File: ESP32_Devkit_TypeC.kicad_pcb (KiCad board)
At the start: 2 copper layers, 25.3 x 48.2 mm, 39 parts, among them J1 USB_C_Receptacle_USB2.0, J2 Conn_01x19, J3 Conn_01x19, Q1 SS8050, Q2 SS8050, SW1 EN, SW2 BOOT, U1 MP2451, U2 CH340G, U3 ESP32-PICO-D4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

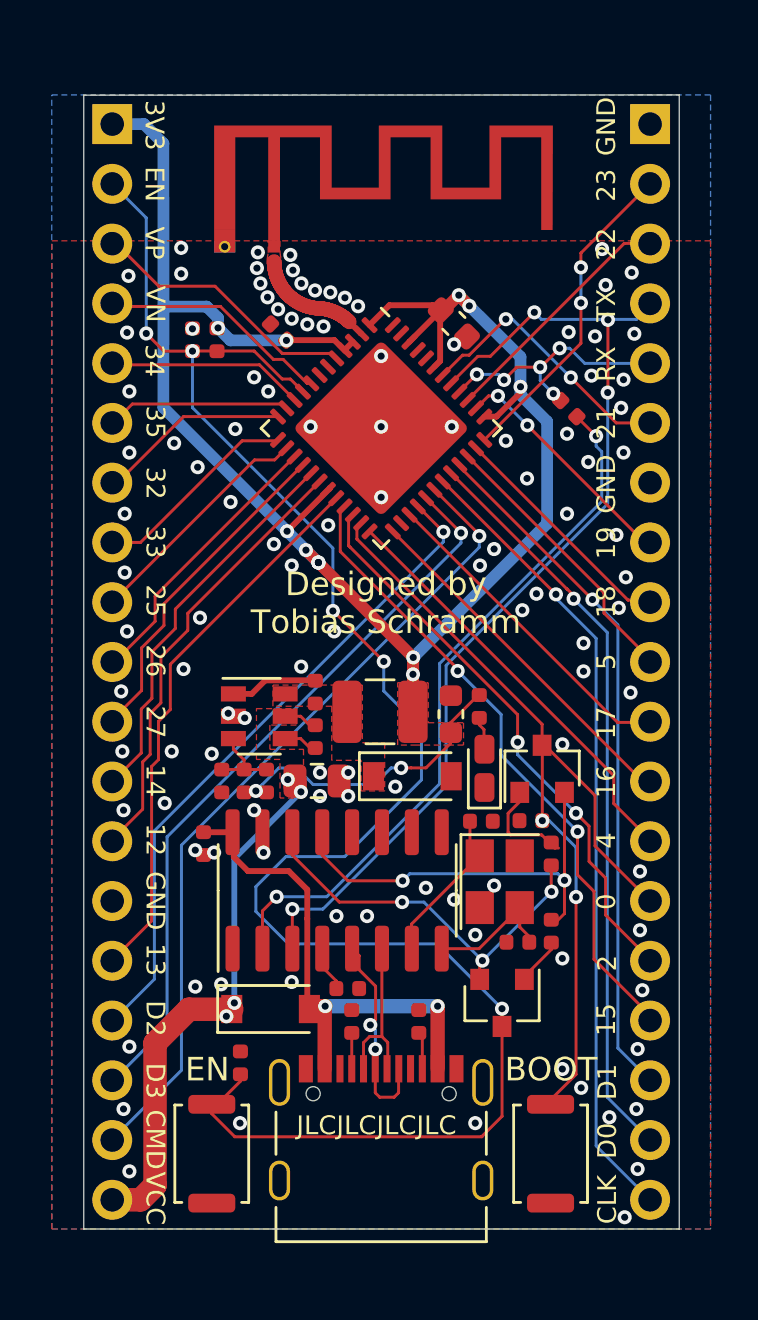
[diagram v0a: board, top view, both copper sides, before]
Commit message: Add silkscreen markings
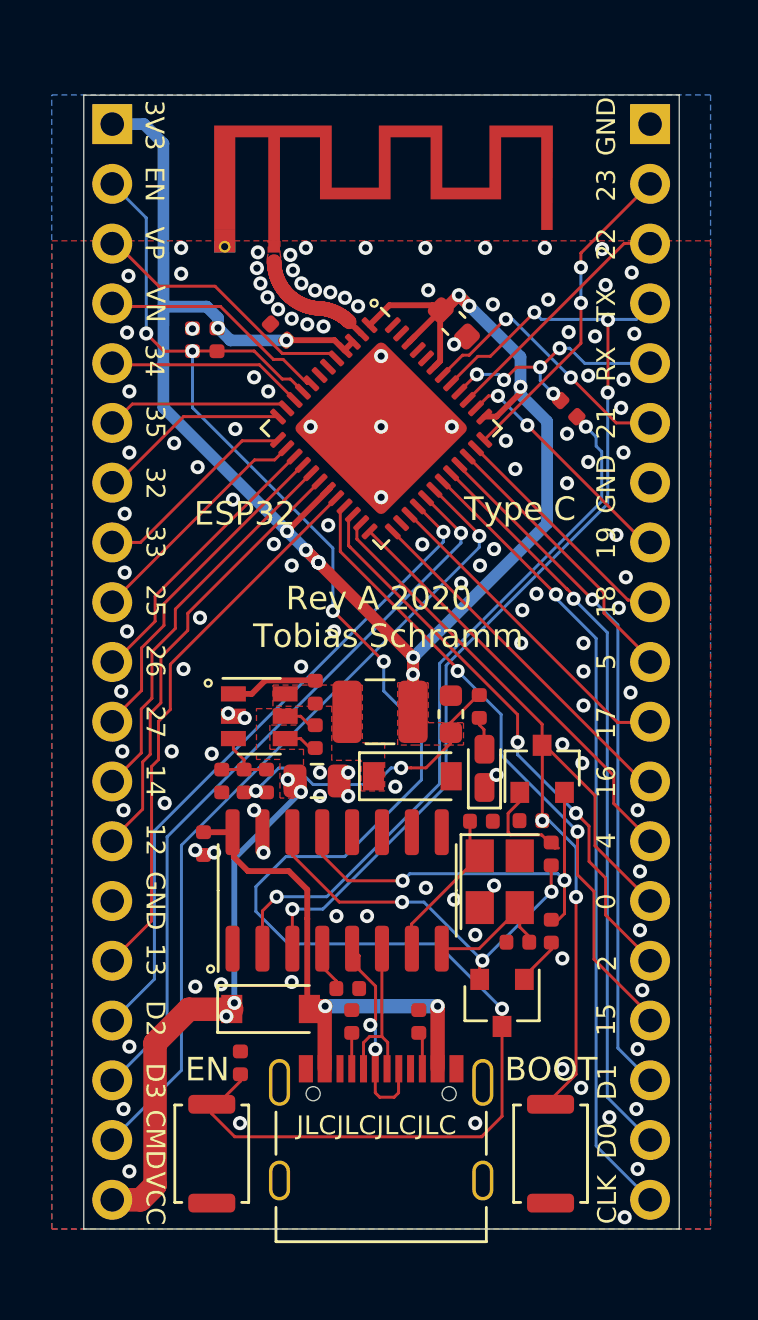
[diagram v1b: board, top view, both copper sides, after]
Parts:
- added I1: Icon, Signs:Danger_RF_Corona, B.Cu at (99.9, 79.9)
- R1: value 100 kR -> 10 kR
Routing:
- net GND: vias 112 -> 127
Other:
- board text added: "ESP32"
- board text added: "Rev A 2020"
- board text added: "Tobias Schramm"
- board text added: "Type C"
- board text removed: "Designed by Tobias Schramm"

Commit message: Add tooling holes
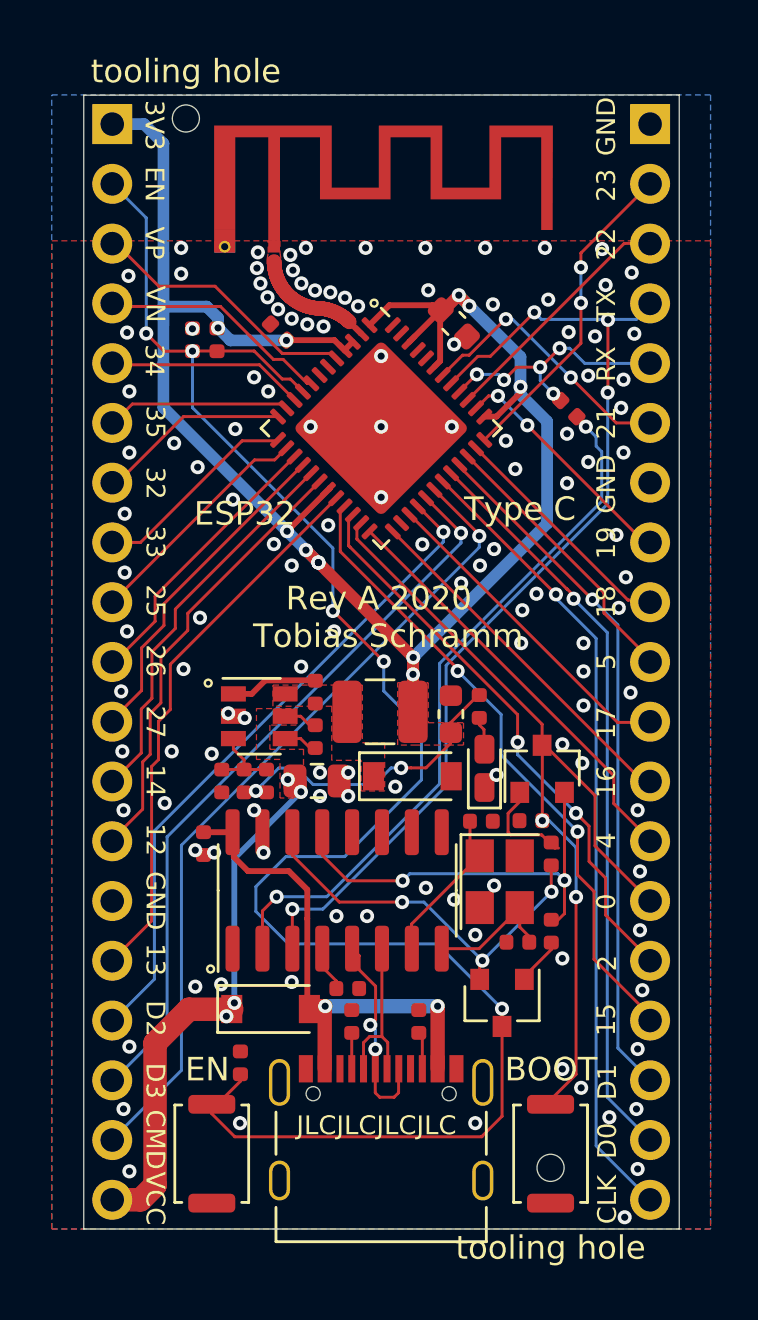
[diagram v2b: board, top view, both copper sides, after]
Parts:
- added H1: MountingHole, ToolingHole:ToolingHole_JLCSMT, F.Cu at (91.7, 76.9)
- added H2: MountingHole, ToolingHole:ToolingHole_JLCSMT, F.Cu at (107.2, 121.5)
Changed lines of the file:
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@@
     (tracks 799)
     (zones 0)
-    (modules 40)
+    (modules 42)
     (nets 69)
   )
@@
     (pcbplotparams
       (layerselection 0x010fc_ffffffff)
-      (usegerberextensions false)
+      (usegerberextensions true)
       (usegerberattributes false)
       (usegerberadvancedattributes false)
@@
       (outputformat 1)
       (mirror false)
-      (drillshape 1)
+      (drillshape 0)
       (scaleselection 1)
-      (outputdirectory ""))
+      (outputdirectory "fab"))
   )
   (net 0 "")
@@
     (add_net VCC)
   )
+  (module ToolingHole:ToolingHole_JLCSMT (layer F.Cu)
+    (at 107.2 121.5)
+    (fp_text reference H2 (at 0 0.5) (layer F.SilkS) hide
+      (effects (font (size 1 1) (thickness 0.15)))
+    )
+    (fp_text value MountingHole (at 0 -0.5) (layer F.Fab)
+      (effects (font (size 1 1) (thickness 0.15)))
+    )
+    (fp_text user "tooling hole" (at 0 3.4) (layer F.SilkS)
+      (effects (font (size 1 1) (thickness 0.15)))
+    )
+    (pad "" np_thru_hole circle (at 0 0) (size 1.152 1.152) (drill 1.152) (layers *.Cu *.Mask))
+  )
+  (module ToolingHole:ToolingHole_JLCSMT (layer F.Cu)
+    (at 91.7 76.9)
+    (fp_text reference H1 (at 0 0.5) (layer F.SilkS) hide
+      (effects (font (size 1 1) (thickness 0.15)))
+    )
+    (fp_text value MountingHole (at 0 -0.5) (layer F.Fab)
+      (effects (font (size 1 1) (thickness 0.15)))
+    )
+    (fp_text user "tooling hole" (at 0 -2) (layer F.SilkS)
+      (effects (font (size 1 1) (thickness 0.15)))
+    )
+    (pad "" np_thru_hole circle (at 0 0) (size 1.152 1.152) (drill 1.152) (layers *.Cu *.Mask))
+  )
   (module Signs:Danger_RF_Corona (layer B.Cu)
     (at 99.9 79.9 180)
@@
     (connect_pads yes (clearance 0.127))
     (min_thickness 0.127)
-    (fill yes (arc_segments 32) (thermal_gap 0.508) (thermal_bridge_width 0.508))
+    (fill (arc_segments 32) (thermal_gap 0.508) (thermal_bridge_width 0.508))
     (polygon
       (pts
@@
     (connect_pads yes (clearance 0.127))
     (min_thickness 0.127)
-    (fill yes (arc_segments 32) (thermal_gap 0.508) (thermal_bridge_width 0.508))
+    (fill (arc_segments 32) (thermal_gap 0.508) (thermal_bridge_width 0.508))
     (polygon
       (pts
@@
     (connect_pads yes (clearance 0.127))
     (min_thickness 0.127)
-    (fill yes (arc_segments 32) (thermal_gap 0.508) (thermal_bridge_width 0.508))
+    (fill (arc_segments 32) (thermal_gap 0.508) (thermal_bridge_width 0.508))
     (polygon
       (pts
@@
     (connect_pads yes (clearance 0.127))
     (min_thickness 0.127)
-    (fill yes (arc_segments 32) (thermal_gap 0.508) (thermal_bridge_width 0.508))
+    (fill (arc_segments 32) (thermal_gap 0.508) (thermal_bridge_width 0.508))
     (polygon
       (pts
@@
     (connect_pads yes (clearance 0.127))
     (min_thickness 0.127)
-    (fill yes (arc_segments 32) (thermal_gap 0.508) (thermal_bridge_width 0.508))
+    (fill (arc_segments 32) (thermal_gap 0.508) (thermal_bridge_width 0.508))
     (polygon
       (pts
@@
     (connect_pads yes (clearance 0.127))
     (min_thickness 0.127)
-    (fill yes (arc_segments 32) (thermal_gap 0.508) (thermal_bridge_width 0.508))
+    (fill (arc_segments 32) (thermal_gap 0.508) (thermal_bridge_width 0.508))
     (polygon
       (pts
